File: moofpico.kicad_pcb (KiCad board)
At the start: 2 copper layers, 85.7 x 62.9 mm, 22 parts, among them J1 Conn_01x04, J100 Bus_Apple_II_Card_Side, J2 Micro_SD_Card_Det2, Q1 BS170, SW1 SW_DIP_x02, U2 74F11, U3 74LVC245, U4 74LVC245, U5 74LVC245, U6 RaspberryPi_Pico

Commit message: more probably needless shuffling around of components
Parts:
- moved R1 2.79 mm to (143.0, 99.6)
- moved Q1 1.55 mm to (175.0, 104.4)
- moved C6 0.74 mm to (140.2, 111.5)
- moved U4 0.24 mm to (135.9, 93.2)
- moved J1 0.19 mm to (107.7, 111.0)
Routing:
- net GND: track 410.3 -> 422.7 mm
- net ENBL: track 69.9 -> 64.8 mm
- net D/OE: track 52.0 -> 56.3 mm
- net DDIR: track 34.2 -> 37.5 mm
- net AD6: track 29.1 -> 27.1 mm
- net AD3: track 28.9 -> 27.2 mm
- net AD7: track 35.7 -> 34.0 mm
- net Net-(J100-~{DEVICE_SELECT}): track 53.5 -> 54.7 mm
- net AD4: track 28.3 -> 27.2 mm
- net AD5: track 28.2 -> 27.2 mm
- net Net-(Q1-G): track 27.5 -> 28.4 mm
- net Net-(J100-~{IRQ}): track 26.4 -> 25.5 mm

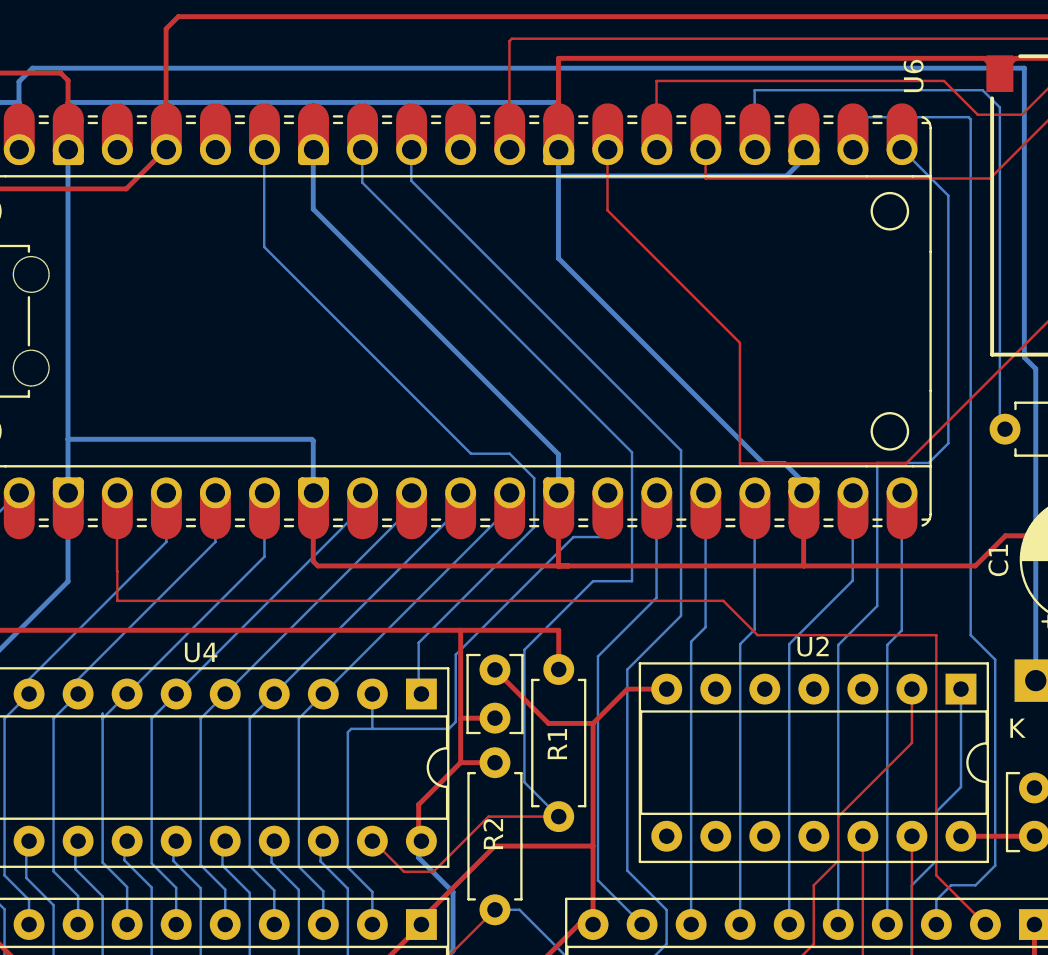
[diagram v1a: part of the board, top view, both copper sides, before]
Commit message: ground unused NAND inputs
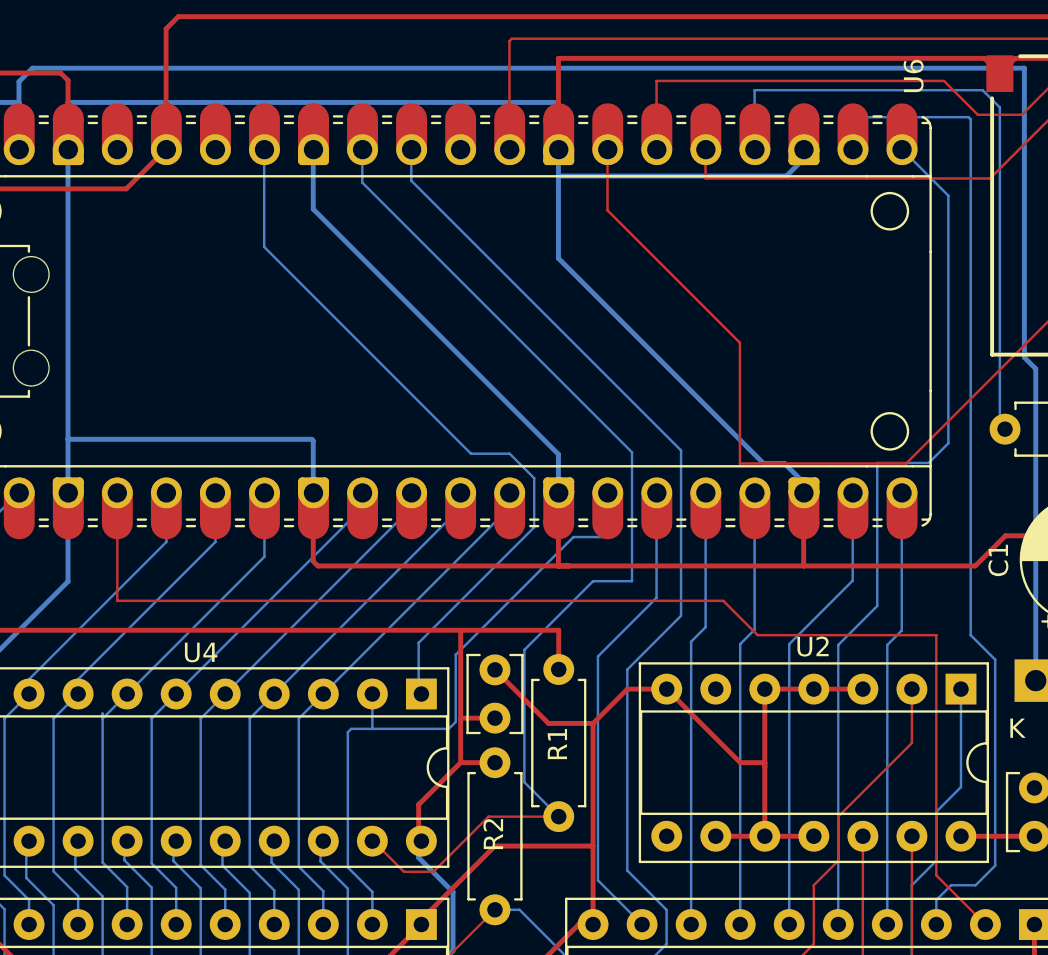
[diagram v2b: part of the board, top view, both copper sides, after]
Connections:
- U2 pad 10: unconnected-(U2-Pad10) -> GND
- U2 pad 11: unconnected-(U2-Pad11) -> GND
- U2 pad 3: unconnected-(U2-Pad3) -> GND
- U2 pad 4: unconnected-(U2-Pad4) -> GND
- U2 pad 5: unconnected-(U2-Pad5) -> GND
- U2 pad 9: unconnected-(U2-Pad9) -> GND
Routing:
- net GND: track 422.7 -> 447.4 mm

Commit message: silkscreening
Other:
- board text added: "GND"
- board text added: "RX UART"
- board text added: "TX UART"
- board text added: "USB PWR"
- board text added: "moofpico ${REVISION}"
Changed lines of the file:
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@@
 			(at -1.564 0 0)
 			(layer "F.SilkS")
+			(hide yes)
 			(effects
 				(font
@@
 			(at 3.81 -3.42 -90)
 			(layer "F.SilkS")
+			(hide yes)
 			(effects
 				(font
@@
 		)
 		(fp_text user "K"
-			(at -1 2.5 0)
+			(at -0.068 2.217 0)
 			(layer "F.SilkS")
 			(effects
@@
 		(fp_arc
 			(start 10.579676 25.189937)
-			(mid 10.357949 25.493953)
+			(mid 10.357946 25.493957)
 			(end 10 25.61)
 			(stroke
@@
 		(layer "Edge.Cuts")
 	)
+	(gr_text "moofpico ${REVISION}"
+		(at 135.636 88.9 0)
+		(layer "F.SilkS")
+		(effects
+			(font
+				(size 0.8128 0.8128)
+				(thickness 0.1524)
+				(bold yes)
+			)
+			(justify left bottom)
+		)
+	)
 	(gr_text "<- KBD"
 		(at 101.84 75.282 0)
 		(layer "F.SilkS")
 		(effects
+			(font
+				(size 0.8128 0.8128)
+				(thickness 0.1524)
+				(bold yes)
+			)
+			(justify left bottom)
+		)
+	)
+	(gr_text "GND"
+		(at 103.632 111.506 0)
+		(layer "F.SilkS")
+		(effects
+			(font
+				(size 0.8128 0.8128)
+				(thickness 0.1524)
+				(bold yes)
+			)
+			(justify left bottom)
+		)
+	)
+	(gr_text "TX UART\n"
+		(at 106.172 107.696 0)
+		(layer "F.SilkS")
+		(effects
+			(font
+				(size 0.8128 0.8128)
+				(thickness 0.1524)
+				(bold yes)
+			)
+			(justify right bottom)
+		)
+	)
+	(gr_text "USB\nPWR"
+		(at 105.918 105.918 0)
+		(layer "F.SilkS")
+		(effects
+			(font
+				(size 0.8128 0.8128)
+				(thickness 0.1524)
+				(bold yes)
+			)
+			(justify left bottom)
+		)
+	)
+	(gr_text "RX UART"
+		(at 100.838 108.966 0)
+		(layer "F.SilkS")
+		(effects

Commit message: muck about with silkscreen; deem version 0.1
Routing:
- net GND: track 447.4 -> 446.4 mm
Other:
- board text added: "JLCJLCJLCJLC"

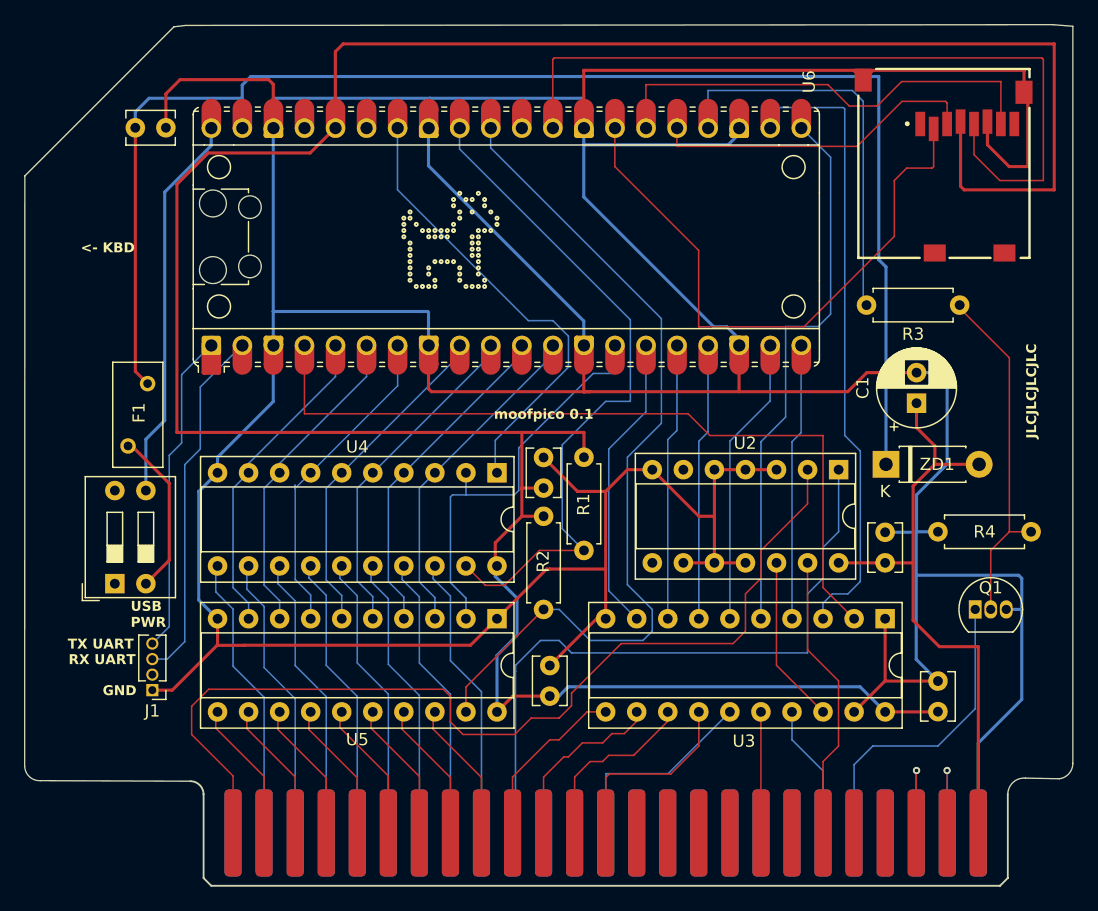
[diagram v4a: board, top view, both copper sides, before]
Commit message: move to 1x dip (even though it's more expensive than 2x?); swap enbl and phi1 to make the pcb layout ever so slightly nicer
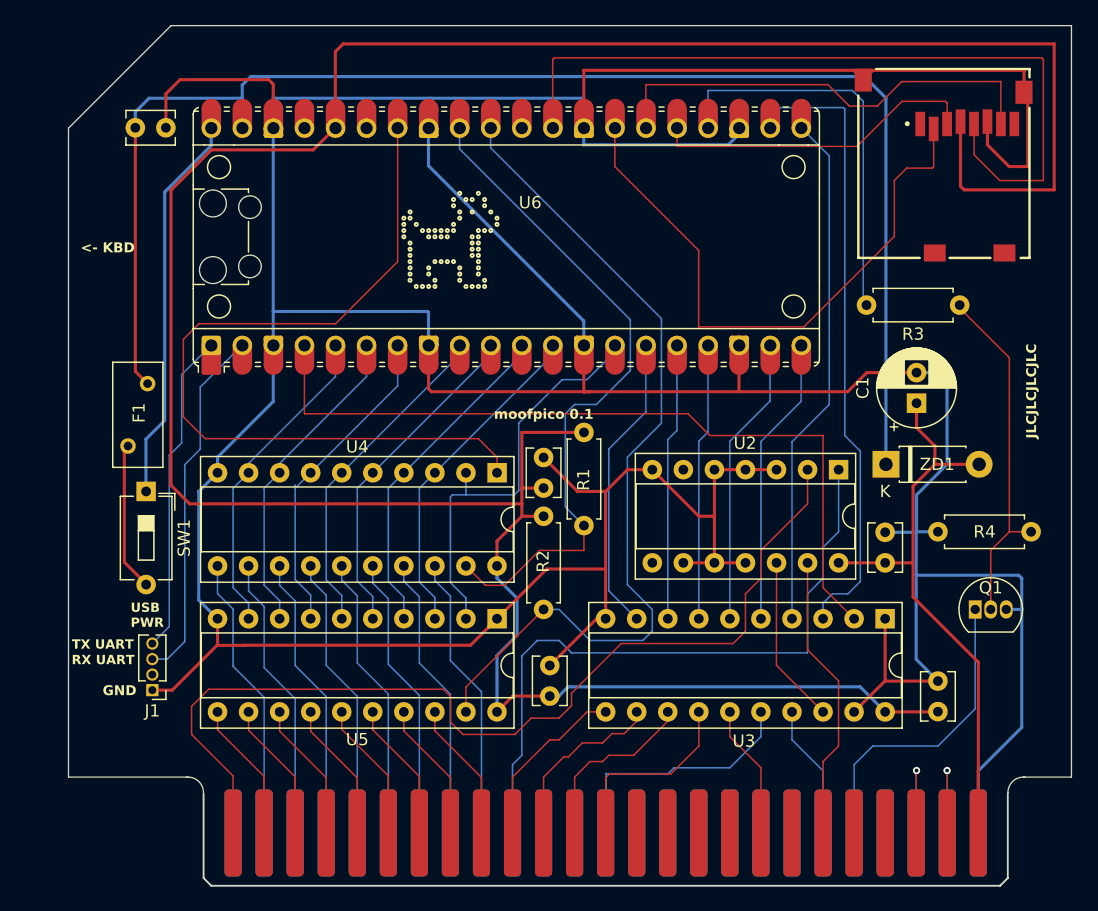
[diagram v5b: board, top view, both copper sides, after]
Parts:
- SW1: value SW_DIP_x02 -> SW_DIP_x01; footprint Button_Switch_THT:SW_DIP_SPSTx02_Slide_9.78x7.26mm_W7.62mm_P2.54mm -> Button_Switch_THT:SW_DIP_SPSTx01_Slide_6.7x4.1mm_W7.62mm_P2.54mm_LowProfile
- moved SW1 7.97 mm to (107.2, 94.7), turned to -90 degrees
- moved R1 2.03 mm to (143.0, 97.5)
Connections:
- SW1 pad 1: unconnected-(SW1-Pad1) -> Net-(U6-VBUS)
- U3 pad 15: TTLPHI1 -> TTLR/W
- U3 pad 16: TTLR/W -> TTLPHI1
- U3 pad 4: R/W -> PHI1
- U3 pad 5: PHI1 -> R/W
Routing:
- net DDIR: track 37.5 -> 65.7 mm
- net GND: track 446.4 -> 424.7 mm
- net TTLPHI1: track 15.3 -> 19.0 mm
- net +3V3: track 227.0 -> 230.5 mm
- net PHI1: track 45.1 -> 42.4 mm
- net +5V: track 50.3 -> 48.4 mm
- net Net-(F1-Pad1): track 13.3 -> 11.7 mm
- net R/W: track 22.7 -> 23.7 mm
- net TTLR/W: track 9.91 -> 11.0 mm
- net Net-(U6-VSYS): track 119.7 -> 119.0 mm
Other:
- board size 85.7 x 62.9 mm -> 82 x 62.9 mm

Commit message: minor fiddling, NFCI
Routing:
- net Net-(F1-Pad1): track 11.7 -> 12.3 mm
- net AD2: track 26.6 -> 26.1 mm
- net AD7: track 34.1 -> 33.6 mm
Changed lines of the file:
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@@
 			)
 		)
-		(property "Description" "1x DIP Switch, Single Pole Single Throw (SPST) switch, small symbol"
+		(property "Description" "Enable USB power for pico when the II is turned off"
 			(at 0 0 -90)
 			(unlocked yes)
@@
 		(fp_arc
 			(start 10.579676 25.189937)
-			(mid 10.357958 25.493991)
+			(mid 10.357949 25.493953)
 			(end 10 25.61)
 			(stroke
@@
 	)
 	(segment
-		(start 144.78 94.742)
-		(end 146.558 92.964)
+		(start 144.78 92.964)
+		(end 148.595 92.964)
 		(width 0.254)
 		(layer "F.Cu")
@@
 	)
 	(segment
-		(start 146.558 92.964)
-		(end 148.595 92.964)
-		(width 0.254)
-		(layer "F.Cu")
-		(net 1)
-	)
-	(segment
 		(start 156.215 100.584)
 		(end 153.675 100.584)
@@
 	)
 	(segment
+		(start 139.7 91.968)
+		(end 140.99 91.968)
+		(width 0.254)
+		(layer "F.Cu")
+		(net 1)
+	)
+	(segment
 		(start 144.78 105.156)
 		(end 144.78 94.742)
@@
 	)
 	(segment
-		(start 142.474 94.742)
-		(end 144.78 94.742)
-		(width 0.254)
-		(layer "F.Cu")
-		(net 1)
-	)
-	(segment
 		(start 153.675 92.964)
 		(end 158.755 92.964)
@@
 	)
 	(segment
+		(start 141.986 92.964)
+		(end 144.78 92.964)
+		(width 0.254)
+		(layer "F.Cu")
+		(net 1)
+	)
+	(segment
 		(start 108.805 62.221)
 		(end 109.968 61.058)
@@
 	)
 	(segment
+		(start 140.99 91.968)
+		(end 141.986 92.964)
+		(width 0.254)
+		(layer "F.Cu")
+		(net 1)
+	)
+	(segment
 		(start 148.595 92.964)
 		(end 152.405 96.774)
@@
 	)
 	(segment
+		(start 144.78 92.964)
+		(end 144.78 94.742)
+		(width 0.254)
+		(layer "F.Cu")
+		(net 1)
+	)
+	(segment
 		(start 165.053 60.296)
 		(end 165.848 61.091)
@@
 	)
 	(segment
-		(start 139.7 91.968)
-		(end 142.474 94.742)
-		(width 0.254)
-		(layer "F.Cu")
-		(net 1)
-	)
-	(segment
 		(start 117.588 61.439)
 		(end 117.588 64.995)
@@
 	)
 	(segment
-		(start 105.41 100.5315)
-		(end 105.41 91.323)
+		(start 105.156 91.577)
+		(end 105.708 91.025)
+		(width 0.254)
+		(layer "F.Cu")
+		(net 4)
+	)
+	(segment
+		(start 105.156 100.2775)
+		(end 105.156 91.577)
 		(width 0.254)
 		(layer "F.Cu")
@@
 	(segment
 		(start 107.169 102.2905)
-		(end 105.41 100.5315)
+		(end 105.156 100.2775)
 		(width 0.254)
 		(layer "F.Cu")
@@
 	)
 	(segment
-		(start 145.542 82.804)
-		(end 145.542 83.312)
-		(width 0.127)
-		(layer "B.Cu")
-		(net 28)
-	)
-	(segment
 		(start 133.35 103.467)
 		(end 132.08 102.197)
@@
 	)
 	(segment
-		(start 120.65 103.217)
-		(end 119.38 101.947)
+		(start 119.38 101.947)
+		(end 119.38 94.488)
 		(width 0.127)
 		(layer "B.Cu")
@@
 	)
 	(segment
-		(start 119.38 94.234)
-		(end 119.38 94.488)
+		(start 120.65 104.883)
+		(end 120.65 103.217)
 		(width 0.127)
 		(layer "B.Cu")
@@
 	)
 	(segment
-		(start 119.38 101.947)
-		(end 119.38 94.234)
-		(width 0.127)
-		(layer "B.Cu")
-		(net 31)
-	)
-	(segment
-		(start 120.65 104.883)
-		(end 120.65 103.217)
+		(start 127.762 82.804)
+		(end 127.762 86.106)
 		(width 0.127)
 		(layer "B.Cu")
@@
 	)
 	(segment
-		(start 127.762 82.804)
-		(end 127.762 86.106)
+		(start 120.65 103.217)
+		(end 119.38 101.947)
 		(width 0.127)
 		(layer "B.Cu")
